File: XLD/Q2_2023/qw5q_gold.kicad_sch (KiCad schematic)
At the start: 127 parts

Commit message: mend
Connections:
- net at Eccosorb?.: now also L:?.; no longer LPF?. (x7)
- net at Eccosorb?.: now also LPF?.; no longer L:?. (x4)
- net at L:?.: now also TWPA?.; no longer Coupler?.
- net at TWPA?.: now also L:?.; no longer L:?.
- net at TJI?.: now also L:?.; no longer L:?. (x2)
- net at L:?.: now also TJI?.
- net at L:?.: now also Coupler?.; no longer TJI?.
- new net: Eccosorb?., LPF?. (x7)
- new net: Eccosorb?., L:?. (x4)
- new net: Coupler?., L:?.
- new net: L:?., TJI?.

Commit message: more updates
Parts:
- removed ATT? (x8): Attenuator 0-Cryo, symbol Quantum Computing:Attenuator 0-Cryo
- added ATT?: Attenuator 10-Cryo, symbol Quantum Computing:Attenuator 3-Cryo
- added ATT?: Attenuator 20-Cryo, symbol Quantum Computing:Attenuator 20-Cryo
- added ATT?: Attenuator 6-Cryo, symbol Quantum Computing:Attenuator 6-Cryo
- added ATT?: Attenuator 1-Cryo, symbol Quantum Computing:Attenuator 0-Cryo
- added ATT?: Attenuator 0-Cryo, symbol Quantum Computing:Attenuator 0-Cryo
- added L:?: SMA-SMA, symbol Quantum Computing:SMA-SMA
- added L:? (x2): COAX-6FT, symbol Quantum Computing:COAX-6FT
- added LX-X?: NbTi-RF-line, symbol Quantum Computing:NbTi-RF-line
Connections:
- net L2-5: now also L:?., L:?.
- net L3-25: now also L:?.
- net L3-28: now also ATT?., ATT?., ATT?., ATT?., ATT?., L:?., L:?., LX-X?.
- net at Eccosorb?.: now also L:?.; no longer LPF?. (x7)
- net at Eccosorb?.: now also LPF?.; no longer L:?. (x4)
- net at L:?.: now also TWPA?.; no longer Coupler?.
- net at TWPA?.: now also L:?.; no longer L:?.
- net at TJI?.: now also L:?.; no longer L:?. (x2)
- net at L:?.: now also Coupler?.; no longer TJI?.
- new net: Eccosorb?., LPF?. (x7)
- new net: Eccosorb?., L:?. (x4)
- new net: Coupler?., L:?.
- new net: L:?., TJI?. (x2)
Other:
- note added: "100mK"
- note added: "1K"
- note added: "20mK"
- note added: "300K"
- note added: "4K"
- note added: "50K"
- note added: "Short Brass"
- note removed: "Small Brass"
- note removed: "argo-11"
- moved on the sheet: ATT?, Eccosorb?, HEMT?, L:?, LO9, LPF?, LX-X?, TJI?, TWPA?

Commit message: update attenuators and pumplines
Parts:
- gave numbers to parts that had none: 118
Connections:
- net at Eccosorb2.: now also L:9.; no longer LPF2.
- net at Eccosorb1.: now also L:7.; no longer LPF1.
- net at Eccosorb7.: now also LPF7.; no longer L:19.
- net at Eccosorb10.: now also LPF10.; no longer L:25.
- net at L:3.: now also TWPA1.; no longer Coupler1.
- net at TWPA1.: now also L:2.; no longer L:3.
- net at Eccosorb6.: now also L:17.; no longer LPF6.
- net at TJI1.: now also L:1.; no longer L:2.
- net at Eccosorb5.: now also LPF5.; no longer L:15.
- net at Eccosorb3.: now also L:11.; no longer LPF3.
- net at Eccosorb9.: now also L:23.; no longer LPF9.
- net at TJI2.: now also L:4.; no longer L:5.
- net at Eccosorb11.: now also LPF11.; no longer L:27.
- net at Eccosorb4.: now also L:13.; no longer LPF4.
- net at Eccosorb8.: now also L:21.; no longer LPF8.
- net at L:4.: now also Coupler1.; no longer TJI2.
- new net: Eccosorb2., LPF2.
- new net: Eccosorb1., LPF1.
- new net: Eccosorb7., L:19.
- new net: Eccosorb10., L:25.
- new net: Coupler1., L:3.
- new net: Eccosorb6., LPF6.
- new net: L:2., TJI1.
- new net: Eccosorb5., L:15.
- new net: Eccosorb3., LPF3.
- new net: Eccosorb9., LPF9.
- new net: L:5., TJI2.
- new net: Eccosorb11., L:27.
- new net: Eccosorb4., LPF4.
- new net: Eccosorb8., LPF8.

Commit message: Improvements to library components, title, date
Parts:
- ATT4: symbol Quantum Computing:Attenuator 0-Cryo -> Quantum Computing:Attenuator 1-Cryo
- ATT8: symbol Quantum Computing:Attenuator 3-Cryo -> Quantum Computing:Attenuator 10-Cryo
- Coupler1: symbol Quantum Computing:QMC-CRYOCOUPLER-20 -> Quantum Computing:Directional Coupler QMC-CRYOCOUPLER-20
- Eccosorb1, Eccosorb2, Eccosorb3, Eccosorb4, Eccosorb5, Eccosorb6: symbol Quantum Computing:IR-10GHz-FF -> Quantum Computing:Filter Eccosorb IR-10GHz-FF
- Eccosorb10, Eccosorb11, Eccosorb7, Eccosorb8, Eccosorb9: symbol Quantum Computing:IR-1GHz-FF -> Quantum Computing:Filter Eccosorb IR-1GHz-FF
- HEMT1: symbol Quantum Computing:LNF-LNC4_8C -> Quantum Computing:Amplifier HEMT LNF-LNC4_8C
- L:1, L:2, L:4: symbol Quantum Computing:SMA-SMA -> Quantum Computing:RF Cable SMA-SMA
- L:10, L:12, L:14, L:16, L:18, L:20, L:22, L:24, L:26, L:6, L:8: value COAX-6FT -> Minicircuits-6FT; symbol Quantum Computing:COAX-6FT -> Quantum Computing:RF Cable Minicircuits-6FT
- L:11, L:13, L:15, L:17, L:19, L:21, L:23, L:25, L:27, L:5, L:7, L:9: symbol Quantum Computing:SMA-SMP -> Quantum Computing:RF Cable SMA-SMP
- L:3: value SMA-SMA_small -> SMA-SMA short; symbol Quantum Computing:SMA-SMA_small -> Quantum Computing:RF Cable SMA-SMA_short
- LPF1: symbol Quantum Computing:F-30-8000-R -> Quantum Computing:Filter Low-Pass F-30-8000-R
- LPF10, LPF11, LPF7, LPF8, LPF9: symbol Quantum Computing:VLFX-1050+ -> Quantum Computing:Filter Low-Pass VLFX-1050+
- LPF2, LPF3, LPF4, LPF5, LPF6: symbol Quantum Computing:VLF-7200+ -> Quantum Computing:Filter Low-Pass VLF-7200+
- LX-X1, LX-X10, LX-X11, LX-X12, LX-X2, LX-X3, LX-X4, LX-X5, LX-X6, LX-X7, LX-X8, LX-X9: value NbTi-RF-line -> NbTi; symbol Quantum Computing:NbTi-RF-line -> Quantum Computing:RF Line NbTi
- QPU1: value qw5q_gold -> QPU QuantWare 5q; symbol Quantum Computing:QPU_5q_flux -> Quantum Computing:QPU QuantWare 5q
- TJI1, TJI2: symbol Quantum Computing:LNF-ISISC4_12A -> Quantum Computing:Isolator LNF-ISISC4_12A
- TWPA1: value SW_TWPA -> TWPA SW; symbol Quantum Computing:SW_TWPA -> Quantum Computing:TWPA SW
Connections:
- net at Eccosorb2.: now also L:9.; no longer LPF2.
- net at Eccosorb1.: now also L:7.; no longer LPF1.
- net at Eccosorb7.: now also LPF7.; no longer L:19.
- net at Eccosorb10.: now also LPF10.; no longer L:25.
- net at L:3.: now also TWPA1.; no longer Coupler1.
- net at TWPA1.: now also L:2.; no longer L:3.
- net at Eccosorb6.: now also L:17.; no longer LPF6.
- net at TJI1.: now also L:1.; no longer L:2.
- net at Eccosorb5.: now also LPF5.; no longer L:15.
- net at Eccosorb3.: now also L:11.; no longer LPF3.
- net at Eccosorb9.: now also L:23.; no longer LPF9.
- net at TJI2.: now also L:4.; no longer L:5.
- net at Eccosorb11.: now also LPF11.; no longer L:27.
- net at Eccosorb4.: now also L:13.; no longer LPF4.
- net at Eccosorb8.: now also L:21.; no longer LPF8.
- net at L:4.: now also Coupler1.; no longer TJI2.
- new net: Eccosorb2., LPF2.
- new net: Eccosorb1., LPF1.
- new net: Eccosorb7., L:19.
- new net: Eccosorb10., L:25.
- new net: Coupler1., L:3.
- new net: Eccosorb6., LPF6.
- new net: L:2., TJI1.
- new net: Eccosorb5., L:15.
- new net: Eccosorb3., LPF3.
- new net: Eccosorb9., LPF9.
- new net: L:5., TJI2.
- new net: Eccosorb11., L:27.
- new net: Eccosorb4., LPF4.
- new net: Eccosorb8., LPF8.
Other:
- note removed: "ISOLATOR-1"
- note removed: "ISOLATOR-2"
- company: (none) -> Technology Innovation Institute
- title: (none) -> XLD Setup Q2 2023

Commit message: Correction in line numbers of QW 25Q
We have checked the cables of QW 25Q by connecting the IN and OUT lines to VNA and found that there is are corrections required in the line numbers mentioned in the drawing. Below are the correction made:

QW P14 - In line L3-30 , Out line L2-1
QW P29 - In line L3-26 , Out line L2-2
QW P44 - In line L3-27 , Out line L2-3
QW P59 - In line L3-18 , Out line L2-4

The Coupler pump line L3-21 replaced with L3-29
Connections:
- net at Eccosorb2.: now also L:9.; no longer LPF2.
- net at Eccosorb1.: now also L:7.; no longer LPF1.
- net at Eccosorb7.: now also LPF7.; no longer L:19.
- net at Eccosorb10.: now also LPF10.; no longer L:25.
- net at L:3.: now also TWPA1.; no longer Coupler1.
- net at TWPA1.: now also L:2.; no longer L:3.
- net at Eccosorb6.: now also L:17.; no longer LPF6.
- net at TJI1.: now also L:1.; no longer L:2.
- net at Eccosorb5.: now also LPF5.; no longer L:15.
- net at Eccosorb3.: now also L:11.; no longer LPF3.
- net at Eccosorb9.: now also L:23.; no longer LPF9.
- net at TJI2.: now also L:4.; no longer L:5.
- net at Eccosorb11.: now also LPF11.; no longer L:27.
- net at Eccosorb4.: now also L:13.; no longer LPF4.
- net at Eccosorb8.: now also L:21.; no longer LPF8.
- net at L:4.: now also Coupler1.; no longer TJI2.
- new net: Eccosorb2., LPF2.
- new net: Eccosorb1., LPF1.
- new net: Eccosorb7., L:19.
- new net: Eccosorb10., L:25.
- new net: Coupler1., L:3.
- new net: Eccosorb6., LPF6.
- new net: L:2., TJI1.
- new net: Eccosorb5., L:15.
- new net: Eccosorb3., LPF3.
- new net: Eccosorb9., LPF9.
- new net: L:5., TJI2.
- new net: Eccosorb11., L:27.
- new net: Eccosorb4., LPF4.
- new net: Eccosorb8., LPF8.

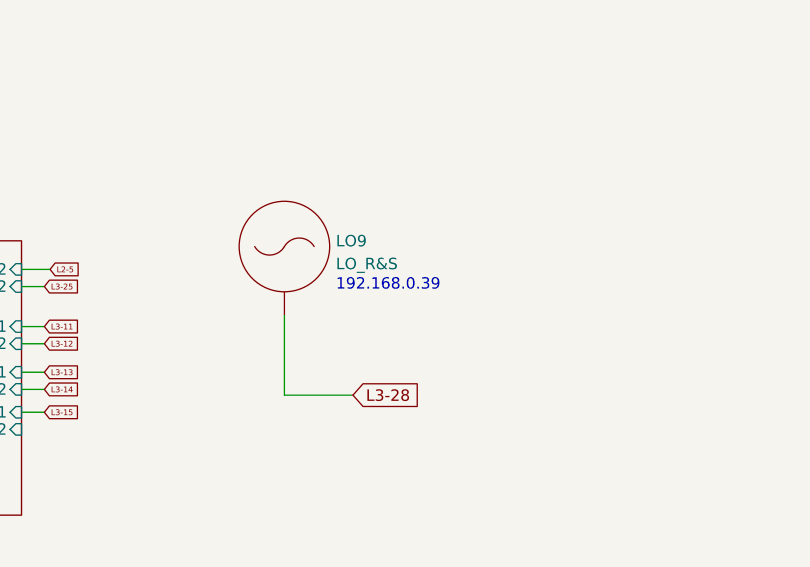
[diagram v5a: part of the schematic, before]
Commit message: fix qw5q twpa pump line ip address
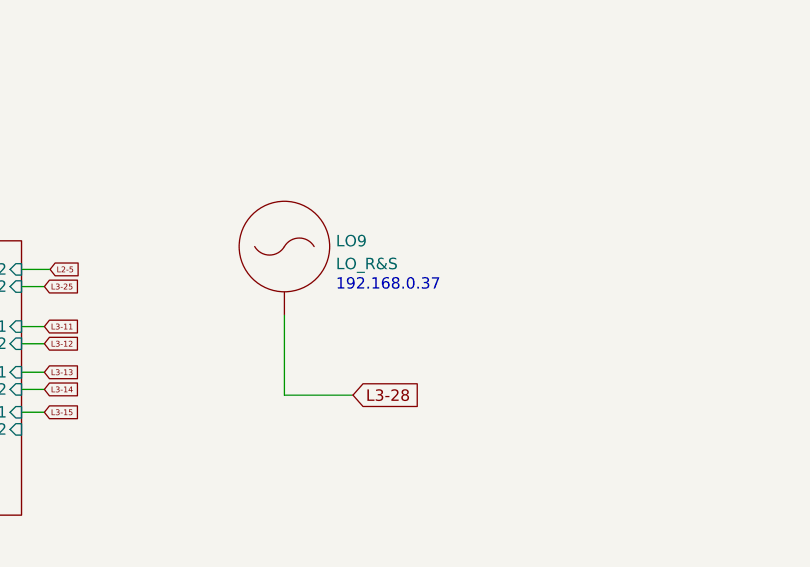
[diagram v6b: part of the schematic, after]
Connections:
- net at Eccosorb2.: now also L:9.; no longer LPF2.
- net at Eccosorb1.: now also L:7.; no longer LPF1.
- net at Eccosorb7.: now also LPF7.; no longer L:19.
- net at Eccosorb10.: now also LPF10.; no longer L:25.
- net at L:3.: now also TWPA1.; no longer Coupler1.
- net at TWPA1.: now also L:2.; no longer L:3.
- net at Eccosorb6.: now also L:17.; no longer LPF6.
- net at TJI1.: now also L:1.; no longer L:2.
- net at Eccosorb5.: now also LPF5.; no longer L:15.
- net at Eccosorb3.: now also L:11.; no longer LPF3.
- net at Eccosorb9.: now also L:23.; no longer LPF9.
- net at TJI2.: now also L:4.; no longer L:5.
- net at Eccosorb11.: now also LPF11.; no longer L:27.
- net at Eccosorb4.: now also L:13.; no longer LPF4.
- net at Eccosorb8.: now also L:21.; no longer LPF8.
- net at L:4.: now also Coupler1.; no longer TJI2.
- new net: Eccosorb2., LPF2.
- new net: Eccosorb1., LPF1.
- new net: Eccosorb7., L:19.
- new net: Eccosorb10., L:25.
- new net: Coupler1., L:3.
- new net: Eccosorb6., LPF6.
- new net: L:2., TJI1.
- new net: Eccosorb5., L:15.
- new net: Eccosorb3., LPF3.
- new net: Eccosorb9., LPF9.
- new net: L:5., TJI2.
- new net: Eccosorb11., L:27.
- new net: Eccosorb4., LPF4.
- new net: Eccosorb8., LPF8.
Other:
- note added: "192.168.0.37"
- note removed: "192.168.0.39"
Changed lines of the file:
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@@
     (stroke (width 0) (type default))
   )
-  (text "192.168.0.39\n" (at 441.325 349.25 0)
+  (text "192.168.0.37\n" (at 441.325 349.25 0)
     (effects (font (size 1.27 1.27)) (justify left bottom))
   )

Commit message: ip for LO18
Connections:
- net at Eccosorb2.: now also L:9.; no longer LPF2.
- net at Eccosorb1.: now also L:7.; no longer LPF1.
- net at Eccosorb7.: now also LPF7.; no longer L:19.
- net at Eccosorb10.: now also LPF10.; no longer L:25.
- net at L:3.: now also TWPA1.; no longer Coupler1.
- net at TWPA1.: now also L:2.; no longer L:3.
- net at Eccosorb6.: now also L:17.; no longer LPF6.
- net at TJI1.: now also L:1.; no longer L:2.
- net at Eccosorb5.: now also LPF5.; no longer L:15.
- net at Eccosorb3.: now also L:11.; no longer LPF3.
- net at Eccosorb9.: now also L:23.; no longer LPF9.
- net at TJI2.: now also L:4.; no longer L:5.
- net at Eccosorb11.: now also LPF11.; no longer L:27.
- net at Eccosorb4.: now also L:13.; no longer LPF4.
- net at Eccosorb8.: now also L:21.; no longer LPF8.
- net at L:4.: now also Coupler1.; no longer TJI2.
- new net: Eccosorb2., LPF2.
- new net: Eccosorb1., LPF1.
- new net: Eccosorb7., L:19.
- new net: Eccosorb10., L:25.
- new net: Coupler1., L:3.
- new net: Eccosorb6., LPF6.
- new net: L:2., TJI1.
- new net: Eccosorb5., L:15.
- new net: Eccosorb3., LPF3.
- new net: Eccosorb9., LPF9.
- new net: L:5., TJI2.
- new net: Eccosorb11., L:27.
- new net: Eccosorb4., LPF4.
- new net: Eccosorb8., LPF8.
